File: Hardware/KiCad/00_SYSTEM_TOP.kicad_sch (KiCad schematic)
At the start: 0 parts

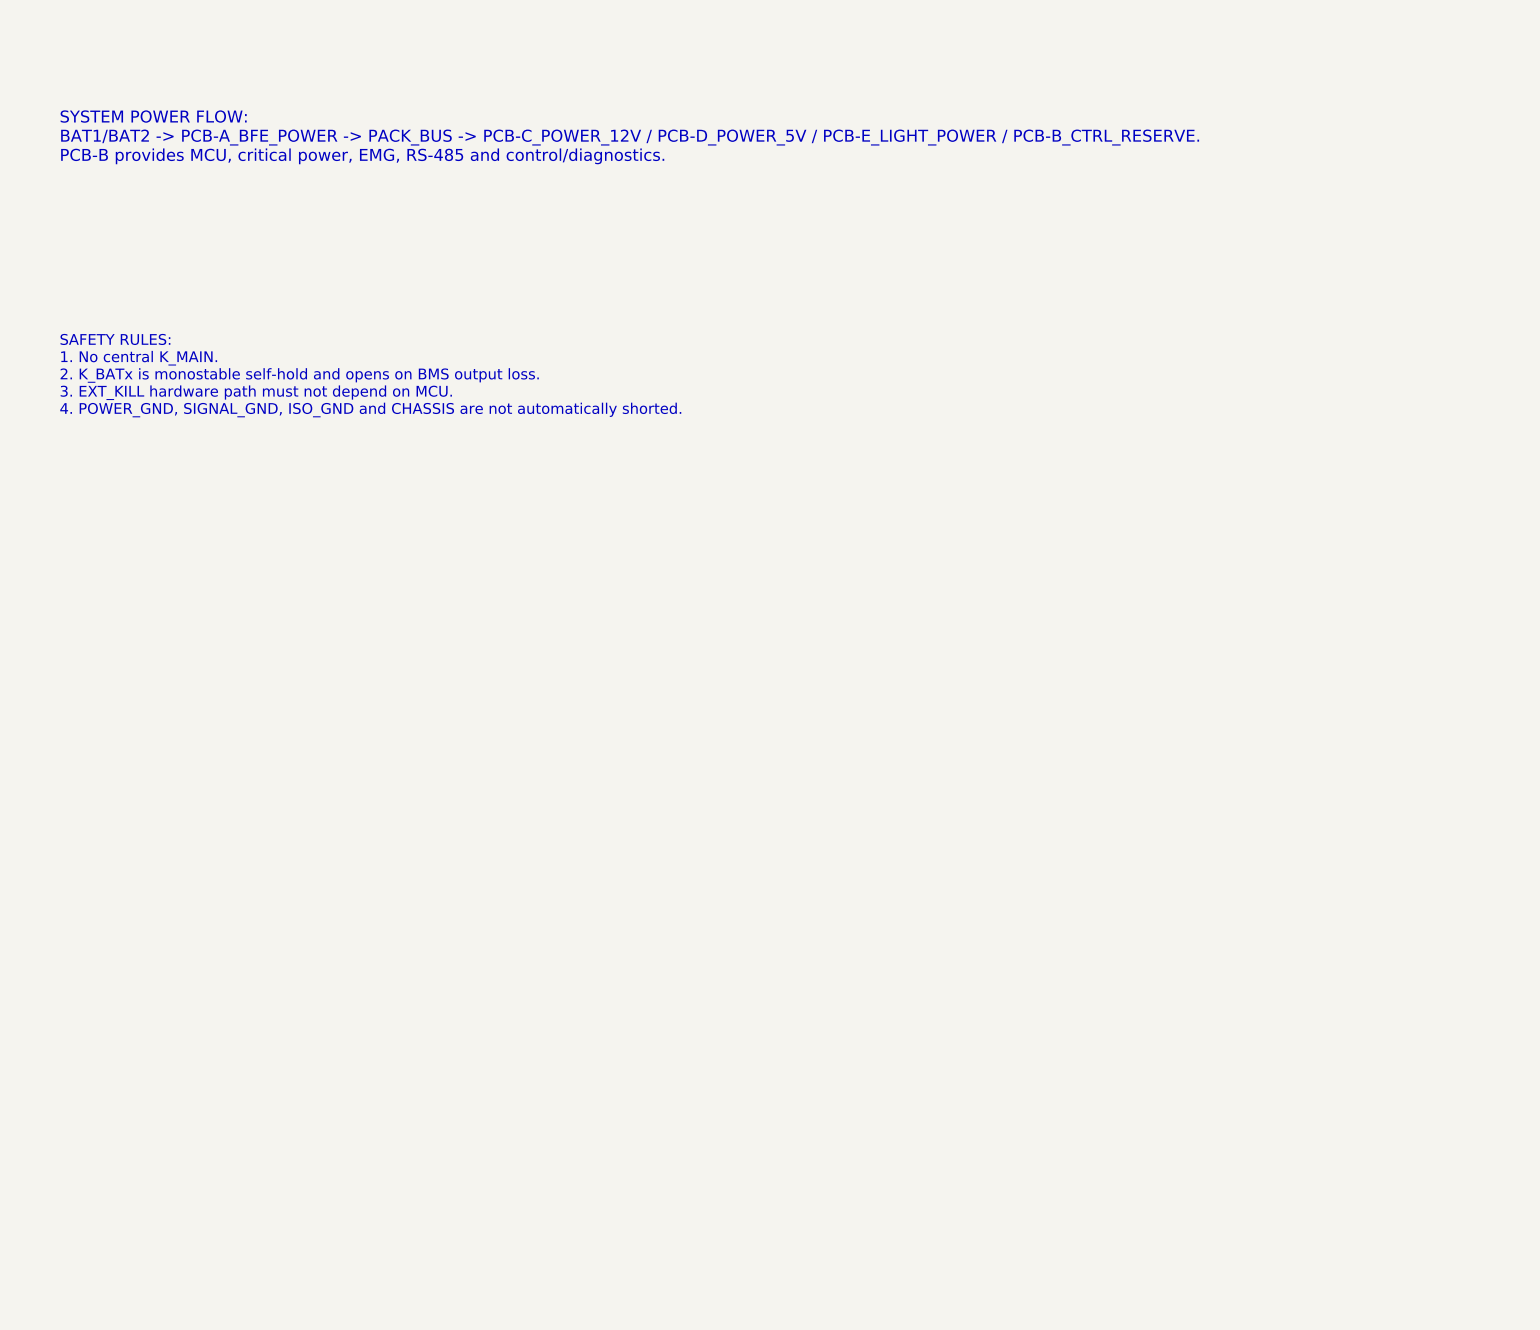
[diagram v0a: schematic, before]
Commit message: hardware: detail 00_SYSTEM_TOP architecture sheet
Accepted working Architecture Level A layout for 00_SYSTEM_TOP.

Notes:
- Adds functional top-level architecture blocks and hierarchical labels.
- Keeps all component selections, footprints and PCB layout out of scope.
- Current visual layout is sufficient for schematic architecture progression, but can be polished later if needed.
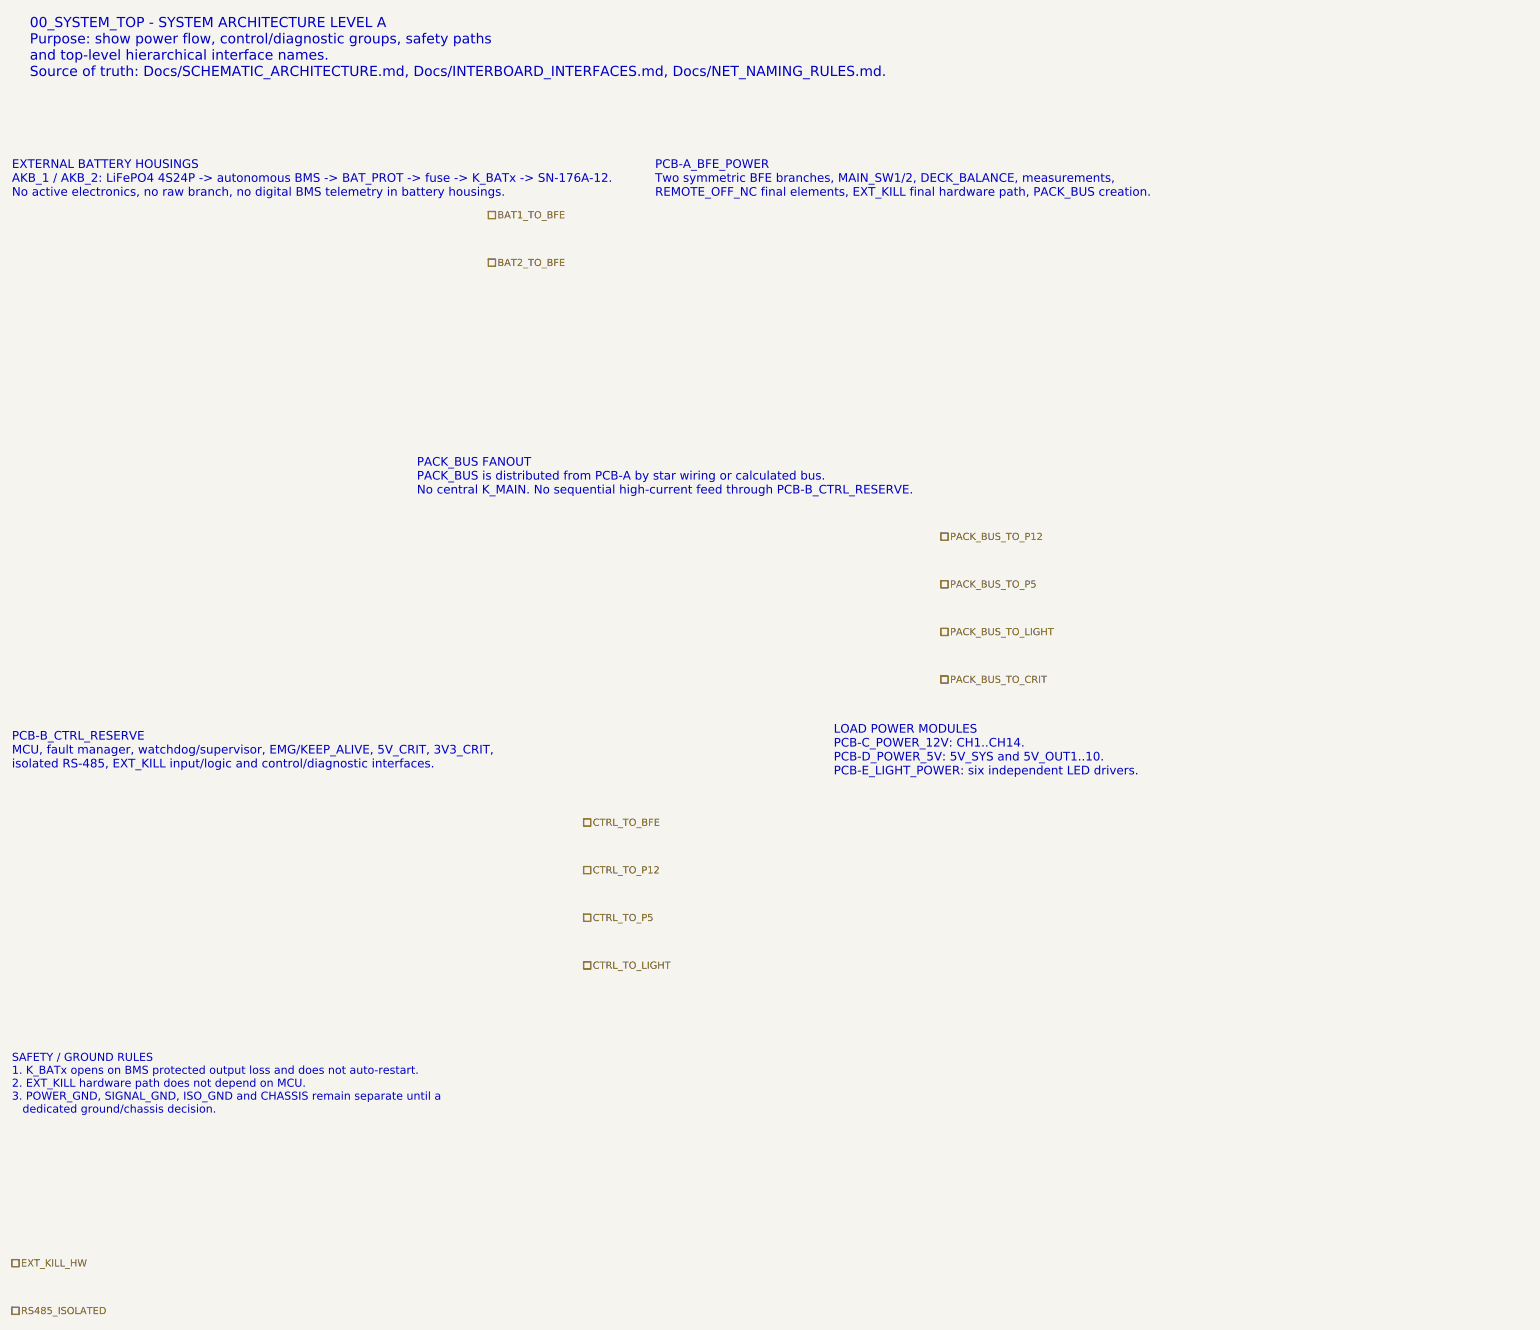
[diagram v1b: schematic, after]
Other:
- note added: "00_SYSTEM_TOP - SYSTEM ARCHITECTURE LEVEL A Purpose: show power flow, control/diagnostic groups, safety paths and top-level hierarchical interface names. Source of truth: Docs/SCHEMATIC_ARCHITECTURE.md, Docs/INTERBOARD_INTERFACES.md, Docs/NET_NAMING_RULES.md."
- note added: "EXTERNAL BATTERY HOUSINGS AKB_1 / AKB_2: LiFePO4 4S24P -> autonomous BMS -> BAT_PROT -> fuse -> K_BATx -> SN-176A-12. No active electronics, no raw branch, no digital BMS telemetry in battery housings."
- note added: "LOAD POWER MODULES PCB-C_POWER_12V: CH1..CH14. PCB-D_POWER_5V: 5V_SYS and 5V_OUT1..10. PCB-E_LIGHT_POWER: six independent LED drivers."
- note added: "PACK_BUS FANOUT PACK_BUS is distributed from PCB-A by star wiring or calculated bus. No central K_MAIN. No sequential high-current feed through PCB-B_CTRL_RESERVE."
- note added: "PCB-A_BFE_POWER Two symmetric BFE branches, MAIN_SW1/2, DECK_BALANCE, measurements, REMOTE_OFF_NC final elements, EXT_KILL final hardware path, PACK_BUS creation."
- note added: "PCB-B_CTRL_RESERVE MCU, fault manager, watchdog/supervisor, EMG/KEEP_ALIVE, 5V_CRIT, 3V3_CRIT, isolated RS-485, EXT_KILL input/logic and control/diagnostic interfaces."
- note added: "SAFETY / GROUND RULES 1. K_BATx opens on BMS protected output loss and does not auto-restart. 2. EXT_KILL hardware path does not depend on MCU. 3. POWER_GND, SIGNAL_GND, ISO_GND and CHASSIS remain separate until a dedicated ground/chassis decision."
- note removed: "SAFETY RULES: 1. No central K_MAIN. 2. K_BATx is monostable self-hold and opens on BMS output loss. 3. EXT_KILL hardware path must not depend on MCU. 4. POWER_GND, SIGNAL_GND, ISO_GND and CHASSIS are not automatically shorted."
- note removed: "SYSTEM POWER FLOW: BAT1/BAT2 -> PCB-A_BFE_POWER -> PACK_BUS -> PCB-C_POWER_12V / PCB-D_POWER_5V / PCB-E_LIGHT_POWER / PCB-B_CTRL_RESERVE. PCB-B provides MCU, critical power, EMG, RS-485 and control/diagnostics."
- company: (none) -> Gonoboben/plataVM
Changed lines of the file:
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@@
 	(title_block
 		(title "00_SYSTEM_TOP - PlataVM system overview")
-		(date "2026-07-14")
-		(rev "A0")
-		(comment 1 "Architecture level A: functional hierarchy, no part numbers")
-	)
-	(text "SYSTEM POWER FLOW:\nBAT1/BAT2 -> PCB-A_BFE_POWER -> PACK_BUS -> PCB-C_POWER_12V / PCB-D_POWER_5V / PCB-E_LIGHT_POWER / PCB-B_CTRL_RESERVE.\nPCB-B provides MCU, critical power, EMG, RS-485 and control/diagnostics."
-		(exclude_from_sim no)
-		(at 20 25 0)
-		(effects
-			(font
-				(size 2 2)
-			)
-			(justify left)
-		)
-	)
-	(text "SAFETY RULES:\n1. No central K_MAIN.\n2. K_BATx is monostable self-hold and opens on BMS output loss.\n3. EXT_KILL hardware path must not depend on MCU.\n4. POWER_GND, SIGNAL_GND, ISO_GND and CHASSIS are not automatically shorted."
-		(exclude_from_sim no)
-		(at 20 65 0)
-		(effects
-			(font
-				(size 1.8 1.8)
-			)
-			(justify left)
+		(date "2026-07-15")
+		(rev "A2")
+		(company "Gonoboben/plataVM")
+		(comment 1 "Architecture Level A: functional blocks and hierarchical labels")
+		(comment 2 "No part numbers, footprints or PCB layout selected on this sheet")
+	)
+	(text "00_SYSTEM_TOP - SYSTEM ARCHITECTURE LEVEL A\nPurpose: show power flow, control/diagnostic groups, safety paths\nand top-level hierarchical interface names.\nSource of truth: Docs/SCHEMATIC_ARCHITECTURE.md, Docs/INTERBOARD_INTERFACES.md, Docs/NET_NAMING_RULES.md."
+		(exclude_from_sim no)
+		(at 15 10 0)
+		(effects
+			(font
+				(size 1.7 1.7)
+			)
+			(justify left)
+		)
+	)
+	(text "EXTERNAL BATTERY HOUSINGS\nAKB_1 / AKB_2: LiFePO4 4S24P -> autonomous BMS -> BAT_PROT -> fuse -> K_BATx -> SN-176A-12.\nNo active electronics, no raw branch, no digital BMS telemetry in battery housings."
+		(exclude_from_sim no)
+		(at 12 32 0)
+		(effects
+			(font
+				(size 1.45 1.45)
+			)
+			(justify left)
+		)
+	)
+	(text "PCB-A_BFE_POWER\nTwo symmetric BFE branches, MAIN_SW1/2, DECK_BALANCE, measurements,\nREMOTE_OFF_NC final elements, EXT_KILL final hardware path, PACK_BUS creation."
+		(exclude_from_sim no)
+		(at 120 32 0)
+		(effects
+			(font
+				(size 1.45 1.45)
+			)
+			(justify left)
+		)
+	)
+	(text "PACK_BUS FANOUT\nPACK_BUS is distributed from PCB-A by star wiring or calculated bus.\nNo central K_MAIN. No sequential high-current feed through PCB-B_CTRL_RESERVE."
+		(exclude_from_sim no)
+		(at 80 82 0)
+		(effects
+			(font
+				(size 1.45 1.45)
+			)
+			(justify left)
+		)
+	)
+	(text "PCB-B_CTRL_RESERVE\nMCU, fault manager, watchdog/supervisor, EMG/KEEP_ALIVE, 5V_CRIT, 3V3_CRIT,\nisolated RS-485, EXT_KILL input/logic and control/diagnostic interfaces."
+		(exclude_from_sim no)
+		(at 12 128 0)
+		(effects
+			(font
+				(size 1.45 1.45)
+			)
+			(justify left)
+		)
+	)
+	(text "LOAD POWER MODULES\nPCB-C_POWER_12V: CH1..CH14.\nPCB-D_POWER_5V: 5V_SYS and 5V_OUT1..10.\nPCB-E_LIGHT_POWER: six independent LED drivers."
+		(exclude_from_sim no)
+		(at 150 128 0)
+		(effects
+			(font
+				(size 1.45 1.45)
+			)
+			(justify left)
+		)
+	)
+	(text "SAFETY / GROUND RULES\n1. K_BATx opens on BMS protected output loss and does not auto-restart.\n2. EXT_KILL hardware path does not depend on MCU.\n3. POWER_GND, SIGNAL_GND, ISO_GND and CHASSIS remain separate until a\n   dedicated ground/chassis decision."
+		(exclude_from_sim no)
+		(at 12 184 0)
+		(effects
+			(font
+				(size 1.35 1.35)
+			)
+			(justify left)
+		)
+	)
+	(hierarchical_label "BAT1_TO_BFE"
+		(shape passive)
+		(exclude_from_sim no)
+		(at 92 38 0)
+		(effects
+			(font
+				(size 1.2 1.2)
+			)
+			(justify left)
+		)
+	)
+	(hierarchical_label "BAT2_TO_BFE"
+		(shape passive)
+		(exclude_from_sim no)
+		(at 92 46 0)
+		(effects
+			(font
+				(size 1.2 1.2)
+			)
+			(justify left)
+		)
+	)
+	(hierarchical_label "PACK_BUS_TO_P12"
+		(shape passive)
+		(exclude_from_sim no)
+		(at 168 92 0)
+		(effects
+			(font
+				(size 1.2 1.2)
+			)
+			(justify left)
+		)
+	)
+	(hierarchical_label "PACK_BUS_TO_P5"
+		(shape passive)
+		(exclude_from_sim no)
+		(at 168 100 0)
+		(effects
+			(font
+				(size 1.2 1.2)
+			)
+			(justify left)
+		)
+	)
+	(hierarchical_label "PACK_BUS_TO_LIGHT"
+		(shape passive)
+		(exclude_from_sim no)
+		(at 168 108 0)
+		(effects
+			(font
+				(size 1.2 1.2)
+			)
+			(justify left)
+		)
+	)
+	(hierarchical_label "PACK_BUS_TO_CRIT"
+		(shape passive)
+		(exclude_from_sim no)
+		(at 168 116 0)
+		(effects
+			(font
+				(size 1.2 1.2)
+			)
+			(justify left)
+		)
+	)
+	(hierarchical_label "CTRL_TO_BFE"
+		(shape passive)
+		(exclude_from_sim no)
+		(at 108 140 0)
+		(effects
+			(font
+				(size 1.2 1.2)
+			)
+			(justify left)
+		)
+	)
+	(hierarchical_label "CTRL_TO_P12"
+		(shape passive)
+		(exclude_from_sim no)
+		(at 108 148 0)
+		(effects
+			(font
+				(size 1.2 1.2)
+			)
+			(justify left)
+		)
+	)
+	(hierarchical_label "CTRL_TO_P5"
+		(shape passive)
+		(exclude_from_sim no)
+		(at 108 156 0)
+		(effects
+			(font
+				(size 1.2 1.2)
+			)
+			(justify left)
+		)
+	)
+	(hierarchical_label "CTRL_TO_LIGHT"
+		(shape passive)
+		(exclude_from_sim no)
+		(at 108 164 0)
+		(effects
+			(font
+				(size 1.2 1.2)
+			)
+			(justify left)
+		)
+	)
+	(hierarchical_label "EXT_KILL_HW"
+		(shape passive)
+		(exclude_from_sim no)
+		(at 12 214 0)
+		(effects
+			(font
+				(size 1.2 1.2)
+			)
+			(justify left)
+		)
+	)
+	(hierarchical_label "RS485_ISOLATED"
+		(shape passive)
+		(exclude_from_sim no)
+		(at 12 222 0)
+		(effects
+			(font
+				(size 1.2 1.2)
+			)
+			(justify left)
